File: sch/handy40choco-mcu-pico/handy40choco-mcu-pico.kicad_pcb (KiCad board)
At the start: 2 copper layers, 175 x 112 mm, 147 parts, among them J1 Conn_01x02, J2 Conn_02x08_Odd_Even, J3 USB_C_Receptacle_USB2.0_16P, J4 Conn_01x04, Q1 DMG2301L, SW1 SW_Push, SW10 SW_Push, SW11 SW_Push, SW12 SW_Push, SW13 SW_Push, SW14 SW_Push, SW15 SW_Push, SW16 SW_Push, SW17 SW_Push, SW18 SW_Push, SW19 SW_Push, SW2 SW_Push, SW20 SW_Push, SW21 SW_Push, SW22 SW_Push, SW23 SW_Push, SW24 SW_Push, SW25 SW_Push, SW26 SW_Push, SW27 SW_Push, SW28 SW_Push, SW29 SW_Push, SW3 SW_Push, SW30 SW_Push, SW31 SW_Push, SW32 SW_Push, SW33 SW_Push, SW34 SW_Push, SW35 SW_Push, SW36 SW_Push, SW37 SW_Push, SW38 SW_Push, SW39 SW_Push, SW4 SW_Push, SW40 SW_Push, SW41 SW_Push, SW42 SW_Push, SW5 SW_Push, SW6 SW_Push, SW7 SW_Push, SW8 SW_Push, SW9 SW_Push, U1 Pico, U2 pimoroni lcd, U3 ESP32-S3-WROOM-1, U4 MIC5219-3.3YM5, Y1 32k

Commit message: マイコン基板(pico)の雛形です。
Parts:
- removed C1: 10u, Capacitor_SMD:C_0603_1608Metric_Pad1.08x0.95mm_HandSolder
- removed C2, C3: 100n, Capacitor_SMD:C_0603_1608Metric_Pad1.08x0.95mm_HandSolder
- removed C4: 1u, Capacitor_SMD:C_0603_1608Metric_Pad1.08x0.95mm_HandSolder
- removed C5: 470p, Capacitor_SMD:C_0603_1608Metric_Pad1.08x0.95mm_HandSolder
- removed C6: 10n, Capacitor_SMD:C_0603_1608Metric_Pad1.08x0.95mm_HandSolder
- removed C7, C8: 15p, Capacitor_SMD:C_0603_1608Metric_Pad1.08x0.95mm_HandSolder
- removed D1, D10, D11, D12, D13, D14, D15, D16, D17, D18, D19, D2, D20, D21, D22, D23, D24, D25, D26, D27, D28, D29, D3, D30, D31, D32, D33, D34, D35, D36, D37, D38, D39, D4, D40, D5, D6, D7, D8, D9: 1N4148W, Diode_SMD:D_SOD-123
- removed D41, D42, D43: D_Schottky, Diode_SMD:D_SOD-123
- removed D44, D45, D46: D_TVS, Diode_SMD:D_SOD-123
- removed D47, D48, D49, D50, D51, D52, D53: LED, LED_SMD:LED_0603_1608Metric_Pad1.05x0.95mm_HandSolder
- removed F1: Polyfuse_Small, Fuse:Fuse_Littelfuse-NANO2-451_453
- removed H1, H10, H11, H12, H13, H14, H2, H3, H4, H5, H6, H7, H8, H9: MountingHole, my_keyswitch:my_MountingHole_2.2mm_M2
- removed J3: USB_C_Receptacle_USB2.0_16P, Connector_USB:USB_C_Receptacle_XKB_U262-16XN-4BVC11
- removed J4: Conn_01x04, Connector_JST:JST_XH_B4B-XH-A_1x04_P2.50mm_Vertical
- removed R1, R11, R12, R2, R8, R9: 0, Resistor_SMD:R_0603_1608Metric
- removed R10: [10M], Resistor_SMD:R_0603_1608Metric
- removed R13, R14, R15, R16, R17, R18, R19: 1k, Resistor_SMD:R_0603_1608Metric
- removed R3, R4, R7: 10k, Resistor_SMD:R_0603_1608Metric
- removed R5, R6: 5.1k, Resistor_SMD:R_0603_1608Metric
- removed SW1, SW10, SW11, SW12, SW13, SW14, SW15, SW16, SW17, SW18, SW19, SW2, SW20, SW21, SW22, SW23, SW24, SW25, SW26, SW27, SW28, SW29, SW3, SW30, SW31, SW32, SW33, SW34, SW35, SW36, SW37, SW38, SW39, SW4, SW40, SW5, SW6, SW7, SW8, SW9: SW_Push, my_keyswitch:SW_Hotswap_Kailh_Choc_V1V2
- removed SW41, SW42: SW_Push, Button_Switch_SMD:SW_Push_SPST_NO_Alps_SKRK
- removed U2: pimoroni lcd, my_pico:pimoroni_lcd_p0.85
- removed U3: ESP32-S3-WROOM-1, RF_Module:ESP32-S3-WROOM-1
- removed U4: MIC5219-3.3YM5, Package_TO_SOT_SMD:SOT-23-5
- removed Y1: 32k, Crystal:Crystal_SMD_2012-2Pin_2.0x1.2mm_HandSoldering
- J2: value Conn_02x08_Odd_Even -> Conn_01x20; footprint my_pico:oled_PinSocket_2x08_P2.54mm_Vertical -> Connector_PinSocket_2.54mm:PinSocket_1x20_P2.54mm_Vertical
- moved J2 98.9 mm to (235.0, 88.0), turned to -90 degrees
- moved Q1 39.3 mm to (170.0, 67.9)
- moved J1 29.8 mm to (172.5, 56.0)
- moved U1 24.2 mm to (210.9, 71.6)
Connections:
- J2 pad 1: GND -> /ROW3
- J2 pad 10: unconnected-(J2-Pin_10-Pad10) -> /COL8
- J2 pad 11: unconnected-(J2-Pin_11-Pad11) -> /COL7
- J2 pad 12: Net-(J2-Pin_12) -> /COL6
- J2 pad 13: Net-(J2-Pin_13) -> GND
- J2 pad 14: /DC -> /COL5
- J2 pad 15: /OLED_RESET -> /COL4
- J2 pad 16: /CS_N -> /COL3
- J2 pad 2: +3.3V -> /ROW2
- J2 pad 3: unconnected-(J2-Pin_3-Pad3) -> GND
- J2 pad 4: /SCLK -> /ROW1
- J2 pad 5: /DATA -> /ROW0
- J2 pad 6: unconnected-(J2-Pin_6-Pad6) -> /COL11
- J2 pad 7: unconnected-(J2-Pin_7-Pad7) -> /COL10
- J2 pad 8: unconnected-(J2-Pin_8-Pad8) -> GND
- J2 pad 9: unconnected-(J2-Pin_9-Pad9) -> /COL9
- U1 pad 1: unconnected-(U1-GPIO0-Pad1)_1 -> /ROW3
- U1 pad 2: unconnected-(U1-GPIO1-Pad2)_1 -> /ROW2
- U1 pad 21: /DC -> unconnected-(U1-GPIO16-Pad21)_1
- U1 pad 22: /CS_N -> unconnected-(U1-GPIO17-Pad22)
- U1 pad 24: /SCLK -> unconnected-(U1-GPIO18-Pad24)
- U1 pad 25: /DATA -> unconnected-(U1-GPIO19-Pad25)
- U1 pad 26: /LCD_BL -> unconnected-(U1-GPIO20-Pad26)
- U1 pad 27: /LCD_TE -> unconnected-(U1-GPIO21-Pad27)_1
- U1 pad 29: /OLED_RESET -> unconnected-(U1-GPIO22-Pad29)_1
- U1 pad 30: /LCD_RESET -> unconnected-(U1-RUN-Pad30)
- U1 pad 4: /ROW3 -> /ROW1
- U1 pad 5: /ROW2 -> /ROW0
- U1 pad 6: /ROW1 -> /COL11
- U1 pad 7: /ROW0 -> /COL10
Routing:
- net /ROW3: track 291.0 -> 0.00 mm, vias 10 -> 0
- net /ROW2: track 274.4 -> 0.00 mm, vias 10 -> 0
- net /ROW1: track 259.9 -> 0.00 mm, vias 10 -> 0
- net /ROW0: track 224.4 -> 0.00 mm, vias 10 -> 0
- net /COL0: track 216.7 -> 0.00 mm
- net /COL1: track 206.4 -> 0.00 mm
- net /COL2: track 186.6 -> 0.00 mm
- net /COL3: track 173.0 -> 0.00 mm
- net +3.3V: track 170.8 -> 0.00 mm, vias 3 -> 0
- net /COL4: track 155.4 -> 0.00 mm
- net /COL5: track 142.1 -> 0.00 mm
- net /COL6: track 132.1 -> 0.00 mm
- net /COL7: track 119.2 -> 0.00 mm
- net /LCD_RESET: track 111.5 -> 0.00 mm
- net /COL8: track 107.2 -> 0.00 mm
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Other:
- board size 175 x 112 mm -> 169.5 x 40 mm
- board text added: "handy40choco mcu pico rev.1"
- board text added: "https://github.com/kenyahiro/handy40choco"
- board text removed: "https://github.com/kenyahiro/mini48-keyboard"
- board text removed: "mini48-keyboard_v2_p17"

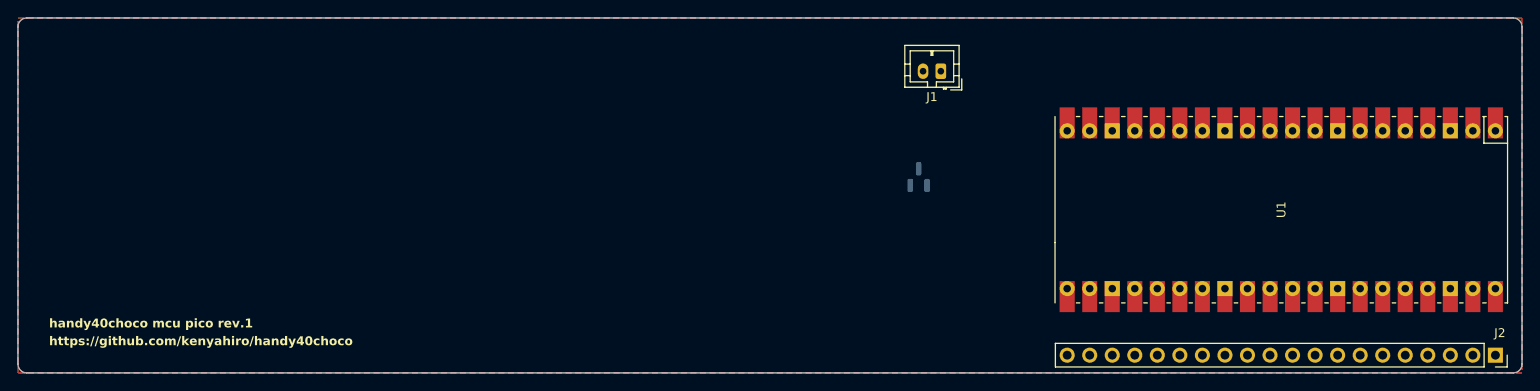
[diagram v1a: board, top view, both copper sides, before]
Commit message: OLEDのコネクタを追加しました。
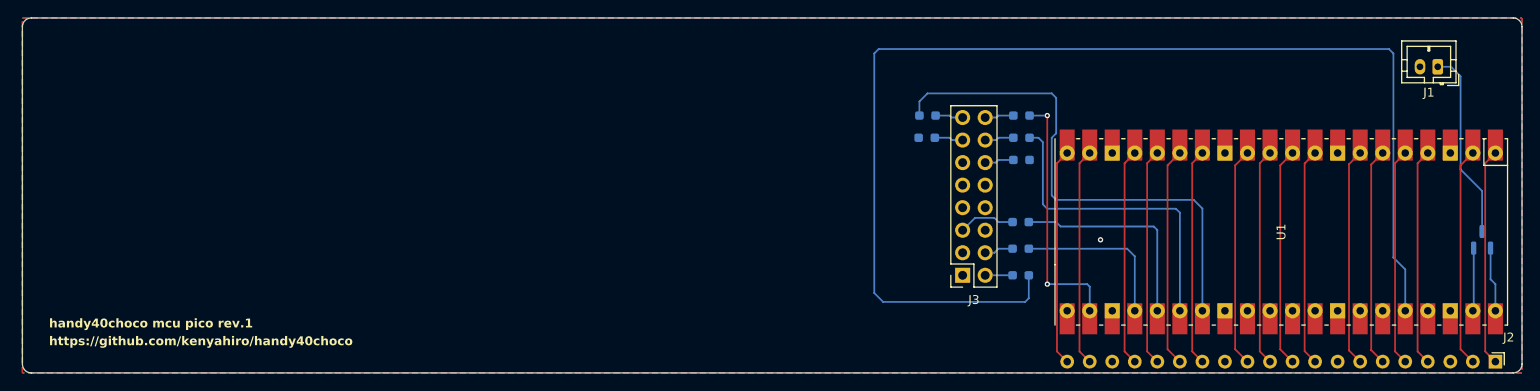
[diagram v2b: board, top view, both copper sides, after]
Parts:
- added J3: Conn_02x08_Odd_Even, my_pico:oled_PinSocket_2x08_P2.54mm_Vertical, F.Cu at (175.0, 79.0)
- added R1: 0, Resistor_SMD:R_0603_1608Metric_Pad0.98x0.95mm_HandSolder, B.Cu at (181.5, 79.0)
- added R2: 1k, Resistor_SMD:R_0603_1608Metric_Pad0.98x0.95mm_HandSolder, B.Cu at (181.6, 66.0)
- added R3: 1k, Resistor_SMD:R_0603_1608Metric_Pad0.98x0.95mm_HandSolder, B.Cu at (170.9, 63.5)
- added R4: 22, Resistor_SMD:R_0603_1608Metric_Pad0.98x0.95mm_HandSolder, B.Cu at (181.6, 61.0)
- added R5: 22, Resistor_SMD:R_0603_1608Metric_Pad0.98x0.95mm_HandSolder, B.Cu at (181.5, 76.0)
- added R6: 22, Resistor_SMD:R_0603_1608Metric_Pad0.98x0.95mm_HandSolder, B.Cu at (181.5, 73.0)
- added R7: 22, Resistor_SMD:R_0603_1608Metric_Pad0.98x0.95mm_HandSolder, B.Cu at (181.6, 63.5)
- added R8: 22, Resistor_SMD:R_0603_1608Metric_Pad0.98x0.95mm_HandSolder, B.Cu at (171.0, 61.0)
- J2: footprint Connector_PinSocket_2.54mm:PinSocket_1x20_P2.54mm_Vertical -> my_keyswitch:my_PinHeader_1x20_P2.54mm_Vertical_p0.85
- moved Q1 63.9 mm to (233.5, 75.0)
- moved J1 56.0 mm to (228.5, 55.5)
- moved U1 2.50 mm to (210.9, 74.1)
- moved J2 0.73 mm to (235.0, 88.7)
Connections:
- U1 pad 22: unconnected-(U1-GPIO17-Pad22) -> Net-(U1-GPIO17)
- U1 pad 24: unconnected-(U1-GPIO18-Pad24) -> Net-(U1-GPIO18)
- U1 pad 25: unconnected-(U1-GPIO19-Pad25) -> Net-(U1-GPIO19)
- U1 pad 26: unconnected-(U1-GPIO20-Pad26) -> Net-(U1-GPIO20)
- U1 pad 27: unconnected-(U1-GPIO21-Pad27)_1 -> Net-(U1-GPIO21)
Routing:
- net +3.3V: track 0.00 -> 136.1 mm
- net Net-(U1-GPIO21): track 0.00 -> 57.9 mm
- net Net-(U1-GPIO20): track 0.00 -> 35.6 mm
- net Net-(U1-GPIO17): track 0.00 -> 28.6 mm, vias 0 -> 2
- net /ROW2: track 0.00 -> 24.7 mm
- net /COL6: track 0.00 -> 24.7 mm
- net /COL4: track 0.00 -> 24.7 mm
- net /COL8: track 0.00 -> 24.7 mm
- net /COL11: track 0.00 -> 24.6 mm
- net /COL10: track 0.00 -> 24.6 mm
- net /COL9: track 0.00 -> 24.5 mm
- net /ROW3: track 0.00 -> 24.5 mm
- net /ROW0: track 0.00 -> 24.5 mm
- net /COL3: track 0.00 -> 24.5 mm
- net /COL2: track 0.00 -> 24.5 mm
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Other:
- board size 169.5 x 40 mm -> 169 x 40 mm

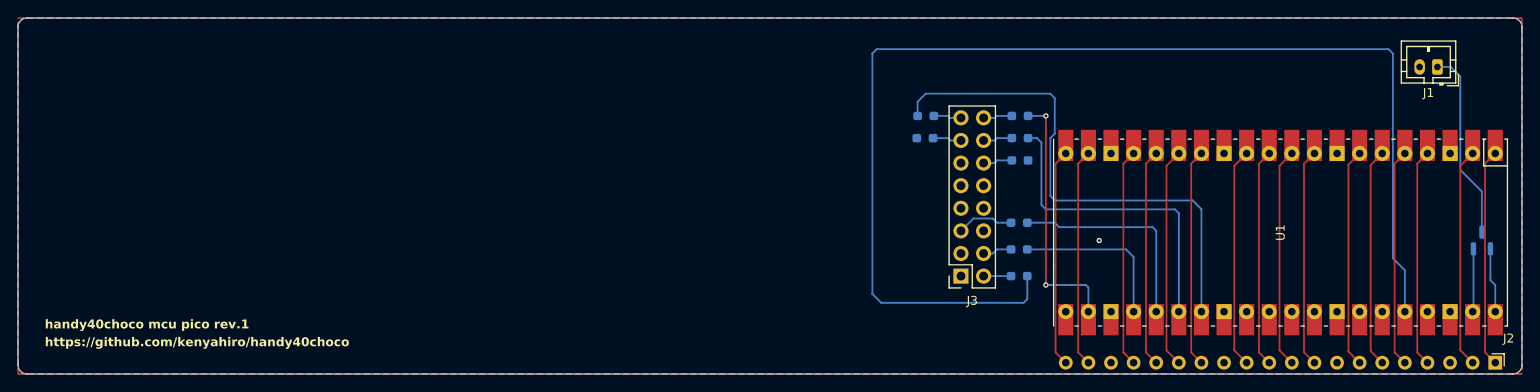
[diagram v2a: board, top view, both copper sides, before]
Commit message: ユニバーサル領域を追加しました。
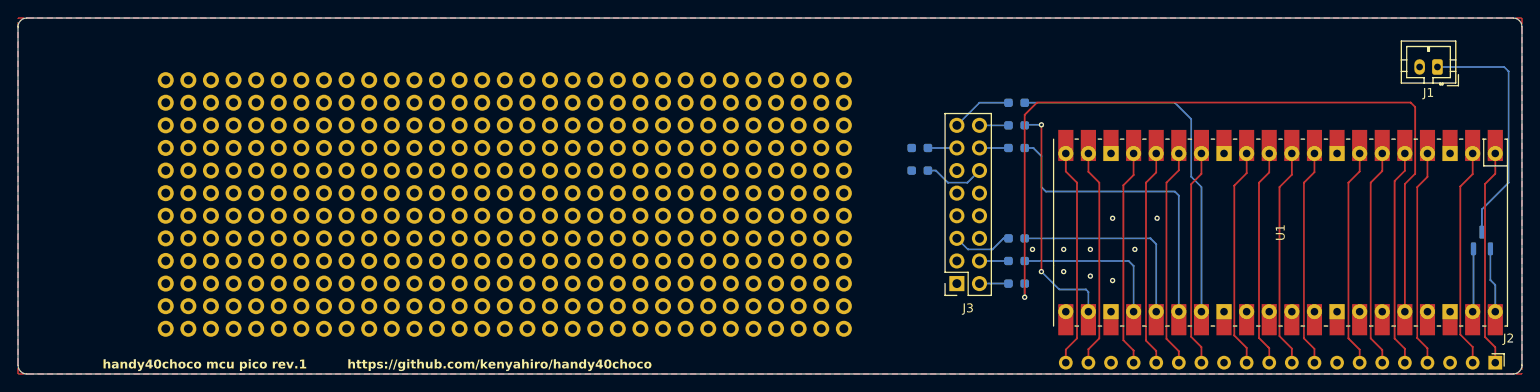
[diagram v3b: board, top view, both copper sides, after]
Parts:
- added H1: MountingHole_Pad, my_keyswitch:TestPoint_THTPad_a, F.Cu at (85.6, 57.0)
- added H10: MountingHole_Pad, my_keyswitch:TestPoint_THTPad_a, F.Cu at (85.6, 79.8)
- added H100: MountingHole_Pad, my_keyswitch:TestPoint_THTPad_a, F.Cu at (105.9, 64.6)
- added H101: MountingHole_Pad, my_keyswitch:TestPoint_THTPad_a, F.Cu at (105.9, 67.1)
- added H102: MountingHole_Pad, my_keyswitch:TestPoint_THTPad_a, F.Cu at (105.9, 69.7)
- added H103: MountingHole_Pad, my_keyswitch:TestPoint_THTPad_a, F.Cu at (105.9, 72.2)
- added H104: MountingHole_Pad, my_keyswitch:TestPoint_THTPad_a, F.Cu at (105.9, 74.8)
- added H105: MountingHole_Pad, my_keyswitch:TestPoint_THTPad_a, F.Cu at (105.9, 77.3)
- added H106: MountingHole_Pad, my_keyswitch:TestPoint_THTPad_a, F.Cu at (105.9, 79.8)
- added H107: MountingHole_Pad, my_keyswitch:TestPoint_THTPad_a, F.Cu at (105.9, 82.4)
- added H108: MountingHole_Pad, my_keyswitch:TestPoint_THTPad_a, F.Cu at (105.9, 84.9)
- added H109: MountingHole_Pad, my_keyswitch:TestPoint_THTPad_a, F.Cu at (108.5, 57.0)
- added H11: MountingHole_Pad, my_keyswitch:TestPoint_THTPad_a, F.Cu at (85.6, 82.4)
- added H110: MountingHole_Pad, my_keyswitch:TestPoint_THTPad_a, F.Cu at (108.5, 59.5)
- added H111: MountingHole_Pad, my_keyswitch:TestPoint_THTPad_a, F.Cu at (108.5, 62.1)
- added H112: MountingHole_Pad, my_keyswitch:TestPoint_THTPad_a, F.Cu at (108.5, 64.6)
- added H113: MountingHole_Pad, my_keyswitch:TestPoint_THTPad_a, F.Cu at (108.5, 67.1)
- added H114: MountingHole_Pad, my_keyswitch:TestPoint_THTPad_a, F.Cu at (108.5, 69.7)
- added H115: MountingHole_Pad, my_keyswitch:TestPoint_THTPad_a, F.Cu at (108.5, 72.2)
- added H116: MountingHole_Pad, my_keyswitch:TestPoint_THTPad_a, F.Cu at (108.5, 74.8)
- added H117: MountingHole_Pad, my_keyswitch:TestPoint_THTPad_a, F.Cu at (108.5, 77.3)
- added H118: MountingHole_Pad, my_keyswitch:TestPoint_THTPad_a, F.Cu at (108.5, 79.8)
- added H119: MountingHole_Pad, my_keyswitch:TestPoint_THTPad_a, F.Cu at (108.5, 82.4)
- added H12: MountingHole_Pad, my_keyswitch:TestPoint_THTPad_a, F.Cu at (85.6, 84.9)
- added H120: MountingHole_Pad, my_keyswitch:TestPoint_THTPad_a, F.Cu at (108.5, 84.9)
- added H121: MountingHole_Pad, my_keyswitch:TestPoint_THTPad_a, F.Cu at (111.0, 57.0)
- added H122: MountingHole_Pad, my_keyswitch:TestPoint_THTPad_a, F.Cu at (111.0, 59.5)
- added H123: MountingHole_Pad, my_keyswitch:TestPoint_THTPad_a, F.Cu at (111.0, 62.1)
- added H124: MountingHole_Pad, my_keyswitch:TestPoint_THTPad_a, F.Cu at (111.0, 64.6)
- added H125: MountingHole_Pad, my_keyswitch:TestPoint_THTPad_a, F.Cu at (111.0, 67.1)
- added H126: MountingHole_Pad, my_keyswitch:TestPoint_THTPad_a, F.Cu at (111.0, 69.7)
- added H127: MountingHole_Pad, my_keyswitch:TestPoint_THTPad_a, F.Cu at (111.0, 72.2)
- added H128: MountingHole_Pad, my_keyswitch:TestPoint_THTPad_a, F.Cu at (111.0, 74.8)
- added H129: MountingHole_Pad, my_keyswitch:TestPoint_THTPad_a, F.Cu at (111.0, 77.3)
- added H13: MountingHole_Pad, my_keyswitch:TestPoint_THTPad_a, F.Cu at (88.1, 57.0)
- added H130: MountingHole_Pad, my_keyswitch:TestPoint_THTPad_a, F.Cu at (111.0, 79.8)
- added H131: MountingHole_Pad, my_keyswitch:TestPoint_THTPad_a, F.Cu at (111.0, 82.4)
- added H132: MountingHole_Pad, my_keyswitch:TestPoint_THTPad_a, F.Cu at (111.0, 84.9)
- added H133: MountingHole_Pad, my_keyswitch:TestPoint_THTPad_a, F.Cu at (113.5, 57.0)
- added H134: MountingHole_Pad, my_keyswitch:TestPoint_THTPad_a, F.Cu at (113.5, 59.5)
- added H135: MountingHole_Pad, my_keyswitch:TestPoint_THTPad_a, F.Cu at (113.5, 62.1)
- added H136: MountingHole_Pad, my_keyswitch:TestPoint_THTPad_a, F.Cu at (113.5, 64.6)
- added H137: MountingHole_Pad, my_keyswitch:TestPoint_THTPad_a, F.Cu at (113.5, 67.1)
- added H138: MountingHole_Pad, my_keyswitch:TestPoint_THTPad_a, F.Cu at (113.5, 69.7)
- added H139: MountingHole_Pad, my_keyswitch:TestPoint_THTPad_a, F.Cu at (113.5, 72.2)
- added H14: MountingHole_Pad, my_keyswitch:TestPoint_THTPad_a, F.Cu at (88.1, 59.5)
- added H140: MountingHole_Pad, my_keyswitch:TestPoint_THTPad_a, F.Cu at (113.5, 74.8)
- added H141: MountingHole_Pad, my_keyswitch:TestPoint_THTPad_a, F.Cu at (113.5, 77.3)
- added H142: MountingHole_Pad, my_keyswitch:TestPoint_THTPad_a, F.Cu at (113.5, 79.8)
- added H143: MountingHole_Pad, my_keyswitch:TestPoint_THTPad_a, F.Cu at (113.5, 82.4)
- added H144: MountingHole_Pad, my_keyswitch:TestPoint_THTPad_a, F.Cu at (113.5, 84.9)
- added H145: MountingHole_Pad, my_keyswitch:TestPoint_THTPad_a, F.Cu at (116.1, 57.0)
- added H146: MountingHole_Pad, my_keyswitch:TestPoint_THTPad_a, F.Cu at (116.1, 59.5)
- added H147: MountingHole_Pad, my_keyswitch:TestPoint_THTPad_a, F.Cu at (116.1, 62.1)
- added H148: MountingHole_Pad, my_keyswitch:TestPoint_THTPad_a, F.Cu at (116.1, 64.6)
- added H149: MountingHole_Pad, my_keyswitch:TestPoint_THTPad_a, F.Cu at (116.1, 67.1)
- added H15: MountingHole_Pad, my_keyswitch:TestPoint_THTPad_a, F.Cu at (88.1, 62.1)
- added H150: MountingHole_Pad, my_keyswitch:TestPoint_THTPad_a, F.Cu at (116.1, 69.7)
- added H151: MountingHole_Pad, my_keyswitch:TestPoint_THTPad_a, F.Cu at (116.1, 72.2)
- added H152: MountingHole_Pad, my_keyswitch:TestPoint_THTPad_a, F.Cu at (116.1, 74.8)
- added H153: MountingHole_Pad, my_keyswitch:TestPoint_THTPad_a, F.Cu at (116.1, 77.3)
- added H154: MountingHole_Pad, my_keyswitch:TestPoint_THTPad_a, F.Cu at (116.1, 79.8)
- added H155: MountingHole_Pad, my_keyswitch:TestPoint_THTPad_a, F.Cu at (116.1, 82.4)
- added H156: MountingHole_Pad, my_keyswitch:TestPoint_THTPad_a, F.Cu at (116.1, 84.9)
- added H157: MountingHole_Pad, my_keyswitch:TestPoint_THTPad_a, F.Cu at (118.6, 57.0)
- added H158: MountingHole_Pad, my_keyswitch:TestPoint_THTPad_a, F.Cu at (118.6, 59.5)
- added H159: MountingHole_Pad, my_keyswitch:TestPoint_THTPad_a, F.Cu at (118.6, 62.1)
- added H16: MountingHole_Pad, my_keyswitch:TestPoint_THTPad_a, F.Cu at (88.1, 64.6)
- added H160: MountingHole_Pad, my_keyswitch:TestPoint_THTPad_a, F.Cu at (118.6, 64.6)
- added H161: MountingHole_Pad, my_keyswitch:TestPoint_THTPad_a, F.Cu at (118.6, 67.1)
- added H162: MountingHole_Pad, my_keyswitch:TestPoint_THTPad_a, F.Cu at (118.6, 69.7)
- added H163: MountingHole_Pad, my_keyswitch:TestPoint_THTPad_a, F.Cu at (118.6, 72.2)
- added H164: MountingHole_Pad, my_keyswitch:TestPoint_THTPad_a, F.Cu at (118.6, 74.8)
- added H165: MountingHole_Pad, my_keyswitch:TestPoint_THTPad_a, F.Cu at (118.6, 77.3)
- added H166: MountingHole_Pad, my_keyswitch:TestPoint_THTPad_a, F.Cu at (118.6, 79.8)
- added H167: MountingHole_Pad, my_keyswitch:TestPoint_THTPad_a, F.Cu at (118.6, 82.4)
- added H168: MountingHole_Pad, my_keyswitch:TestPoint_THTPad_a, F.Cu at (118.6, 84.9)
- added H169: MountingHole_Pad, my_keyswitch:TestPoint_THTPad_a, F.Cu at (121.2, 57.0)
- added H17: MountingHole_Pad, my_keyswitch:TestPoint_THTPad_a, F.Cu at (88.1, 67.1)
- added H170: MountingHole_Pad, my_keyswitch:TestPoint_THTPad_a, F.Cu at (121.2, 59.5)
- added H171: MountingHole_Pad, my_keyswitch:TestPoint_THTPad_a, F.Cu at (121.2, 62.1)
- added H172: MountingHole_Pad, my_keyswitch:TestPoint_THTPad_a, F.Cu at (121.2, 64.6)
- added H173: MountingHole_Pad, my_keyswitch:TestPoint_THTPad_a, F.Cu at (121.2, 67.1)
- added H174: MountingHole_Pad, my_keyswitch:TestPoint_THTPad_a, F.Cu at (121.2, 69.7)
- added H175: MountingHole_Pad, my_keyswitch:TestPoint_THTPad_a, F.Cu at (121.2, 72.2)
- added H176: MountingHole_Pad, my_keyswitch:TestPoint_THTPad_a, F.Cu at (121.2, 74.8)
- added H177: MountingHole_Pad, my_keyswitch:TestPoint_THTPad_a, F.Cu at (121.2, 77.3)
- added H178: MountingHole_Pad, my_keyswitch:TestPoint_THTPad_a, F.Cu at (121.2, 79.8)
- added H179: MountingHole_Pad, my_keyswitch:TestPoint_THTPad_a, F.Cu at (121.2, 82.4)
- added H18: MountingHole_Pad, my_keyswitch:TestPoint_THTPad_a, F.Cu at (88.1, 69.7)
- added H180: MountingHole_Pad, my_keyswitch:TestPoint_THTPad_a, F.Cu at (121.2, 84.9)
- added H181: MountingHole_Pad, my_keyswitch:TestPoint_THTPad_a, F.Cu at (123.7, 57.0)
- added H182: MountingHole_Pad, my_keyswitch:TestPoint_THTPad_a, F.Cu at (123.7, 59.5)
- added H183: MountingHole_Pad, my_keyswitch:TestPoint_THTPad_a, F.Cu at (123.7, 62.1)
- added H184: MountingHole_Pad, my_keyswitch:TestPoint_THTPad_a, F.Cu at (123.7, 64.6)
- added H185: MountingHole_Pad, my_keyswitch:TestPoint_THTPad_a, F.Cu at (123.7, 67.1)
- added H186: MountingHole_Pad, my_keyswitch:TestPoint_THTPad_a, F.Cu at (123.7, 69.7)
- added H187: MountingHole_Pad, my_keyswitch:TestPoint_THTPad_a, F.Cu at (123.7, 72.2)
- added H188: MountingHole_Pad, my_keyswitch:TestPoint_THTPad_a, F.Cu at (123.7, 74.8)
- added H189: MountingHole_Pad, my_keyswitch:TestPoint_THTPad_a, F.Cu at (123.7, 77.3)
- added H19: MountingHole_Pad, my_keyswitch:TestPoint_THTPad_a, F.Cu at (88.1, 72.2)
- added H190: MountingHole_Pad, my_keyswitch:TestPoint_THTPad_a, F.Cu at (123.7, 79.8)
- added H191: MountingHole_Pad, my_keyswitch:TestPoint_THTPad_a, F.Cu at (123.7, 82.4)
- added H192: MountingHole_Pad, my_keyswitch:TestPoint_THTPad_a, F.Cu at (123.7, 84.9)
- added H193: MountingHole_Pad, my_keyswitch:TestPoint_THTPad_a, F.Cu at (126.2, 57.0)
- added H194: MountingHole_Pad, my_keyswitch:TestPoint_THTPad_a, F.Cu at (126.2, 59.5)
- added H195: MountingHole_Pad, my_keyswitch:TestPoint_THTPad_a, F.Cu at (126.2, 62.1)
- added H196: MountingHole_Pad, my_keyswitch:TestPoint_THTPad_a, F.Cu at (126.2, 64.6)
- added H197: MountingHole_Pad, my_keyswitch:TestPoint_THTPad_a, F.Cu at (126.2, 67.1)
- added H198: MountingHole_Pad, my_keyswitch:TestPoint_THTPad_a, F.Cu at (126.2, 69.7)
- added H199: MountingHole_Pad, my_keyswitch:TestPoint_THTPad_a, F.Cu at (126.2, 72.2)
- added H2: MountingHole_Pad, my_keyswitch:TestPoint_THTPad_a, F.Cu at (85.6, 59.5)
- added H20: MountingHole_Pad, my_keyswitch:TestPoint_THTPad_a, F.Cu at (88.1, 74.8)
- added H200: MountingHole_Pad, my_keyswitch:TestPoint_THTPad_a, F.Cu at (126.2, 74.8)
- added H201: MountingHole_Pad, my_keyswitch:TestPoint_THTPad_a, F.Cu at (126.2, 77.3)
- added H202: MountingHole_Pad, my_keyswitch:TestPoint_THTPad_a, F.Cu at (126.2, 79.8)
- added H203: MountingHole_Pad, my_keyswitch:TestPoint_THTPad_a, F.Cu at (126.2, 82.4)
- added H204: MountingHole_Pad, my_keyswitch:TestPoint_THTPad_a, F.Cu at (126.2, 84.9)
- added H205: MountingHole_Pad, my_keyswitch:TestPoint_THTPad_a, F.Cu at (128.8, 57.0)
- added H206: MountingHole_Pad, my_keyswitch:TestPoint_THTPad_a, F.Cu at (128.8, 59.5)
- added H207: MountingHole_Pad, my_keyswitch:TestPoint_THTPad_a, F.Cu at (128.8, 62.1)
- added H208: MountingHole_Pad, my_keyswitch:TestPoint_THTPad_a, F.Cu at (128.8, 64.6)
- added H209: MountingHole_Pad, my_keyswitch:TestPoint_THTPad_a, F.Cu at (128.8, 67.1)
- added H21: MountingHole_Pad, my_keyswitch:TestPoint_THTPad_a, F.Cu at (88.1, 77.3)
- added H210: MountingHole_Pad, my_keyswitch:TestPoint_THTPad_a, F.Cu at (128.8, 69.7)
- added H211: MountingHole_Pad, my_keyswitch:TestPoint_THTPad_a, F.Cu at (128.8, 72.2)
- added H212: MountingHole_Pad, my_keyswitch:TestPoint_THTPad_a, F.Cu at (128.8, 74.8)
- added H213: MountingHole_Pad, my_keyswitch:TestPoint_THTPad_a, F.Cu at (128.8, 77.3)
- added H214: MountingHole_Pad, my_keyswitch:TestPoint_THTPad_a, F.Cu at (128.8, 79.8)
- added H215: MountingHole_Pad, my_keyswitch:TestPoint_THTPad_a, F.Cu at (128.8, 82.4)
- added H216: MountingHole_Pad, my_keyswitch:TestPoint_THTPad_a, F.Cu at (128.8, 84.9)
- added H217: MountingHole_Pad, my_keyswitch:TestPoint_THTPad_a, F.Cu at (131.3, 57.0)
- added H218: MountingHole_Pad, my_keyswitch:TestPoint_THTPad_a, F.Cu at (131.3, 59.5)
- added H219: MountingHole_Pad, my_keyswitch:TestPoint_THTPad_a, F.Cu at (131.3, 62.1)
- added H22: MountingHole_Pad, my_keyswitch:TestPoint_THTPad_a, F.Cu at (88.1, 79.8)
- added H220: MountingHole_Pad, my_keyswitch:TestPoint_THTPad_a, F.Cu at (131.3, 64.6)
- added H221: MountingHole_Pad, my_keyswitch:TestPoint_THTPad_a, F.Cu at (131.3, 67.1)
- added H222: MountingHole_Pad, my_keyswitch:TestPoint_THTPad_a, F.Cu at (131.3, 69.7)
- added H223: MountingHole_Pad, my_keyswitch:TestPoint_THTPad_a, F.Cu at (131.3, 72.2)
- added H224: MountingHole_Pad, my_keyswitch:TestPoint_THTPad_a, F.Cu at (131.3, 74.8)
- added H225: MountingHole_Pad, my_keyswitch:TestPoint_THTPad_a, F.Cu at (131.3, 77.3)
- added H226: MountingHole_Pad, my_keyswitch:TestPoint_THTPad_a, F.Cu at (131.3, 79.8)
- added H227: MountingHole_Pad, my_keyswitch:TestPoint_THTPad_a, F.Cu at (131.3, 82.4)
- added H228: MountingHole_Pad, my_keyswitch:TestPoint_THTPad_a, F.Cu at (131.3, 84.9)
- added H229: MountingHole_Pad, my_keyswitch:TestPoint_THTPad_a, F.Cu at (133.9, 57.0)
- added H23: MountingHole_Pad, my_keyswitch:TestPoint_THTPad_a, F.Cu at (88.1, 82.4)
- added H230: MountingHole_Pad, my_keyswitch:TestPoint_THTPad_a, F.Cu at (133.9, 59.5)
- added H231: MountingHole_Pad, my_keyswitch:TestPoint_THTPad_a, F.Cu at (133.9, 62.1)
- added H232: MountingHole_Pad, my_keyswitch:TestPoint_THTPad_a, F.Cu at (133.9, 64.6)
- added H233: MountingHole_Pad, my_keyswitch:TestPoint_THTPad_a, F.Cu at (133.9, 67.1)
- added H234: MountingHole_Pad, my_keyswitch:TestPoint_THTPad_a, F.Cu at (133.9, 69.7)
- added H235: MountingHole_Pad, my_keyswitch:TestPoint_THTPad_a, F.Cu at (133.9, 72.2)
- added H236: MountingHole_Pad, my_keyswitch:TestPoint_THTPad_a, F.Cu at (133.9, 74.8)
- added H237: MountingHole_Pad, my_keyswitch:TestPoint_THTPad_a, F.Cu at (133.9, 77.3)
- added H238: MountingHole_Pad, my_keyswitch:TestPoint_THTPad_a, F.Cu at (133.9, 79.8)
- added H239: MountingHole_Pad, my_keyswitch:TestPoint_THTPad_a, F.Cu at (133.9, 82.4)
- added H24: MountingHole_Pad, my_keyswitch:TestPoint_THTPad_a, F.Cu at (88.1, 84.9)
- added H240: MountingHole_Pad, my_keyswitch:TestPoint_THTPad_a, F.Cu at (133.9, 84.9)
- added H241: MountingHole_Pad, my_keyswitch:TestPoint_THTPad_a, F.Cu at (136.4, 57.0)
- added H242: MountingHole_Pad, my_keyswitch:TestPoint_THTPad_a, F.Cu at (136.4, 59.5)
- added H243: MountingHole_Pad, my_keyswitch:TestPoint_THTPad_a, F.Cu at (136.4, 62.1)
- added H244: MountingHole_Pad, my_keyswitch:TestPoint_THTPad_a, F.Cu at (136.4, 64.6)
- added H245: MountingHole_Pad, my_keyswitch:TestPoint_THTPad_a, F.Cu at (136.4, 67.1)
- added H246: MountingHole_Pad, my_keyswitch:TestPoint_THTPad_a, F.Cu at (136.4, 69.7)
- added H247: MountingHole_Pad, my_keyswitch:TestPoint_THTPad_a, F.Cu at (136.4, 72.2)
- added H248: MountingHole_Pad, my_keyswitch:TestPoint_THTPad_a, F.Cu at (136.4, 74.8)
- added H249: MountingHole_Pad, my_keyswitch:TestPoint_THTPad_a, F.Cu at (136.4, 77.3)
- added H25: MountingHole_Pad, my_keyswitch:TestPoint_THTPad_a, F.Cu at (90.7, 57.0)
- added H250: MountingHole_Pad, my_keyswitch:TestPoint_THTPad_a, F.Cu at (136.4, 79.8)
- added H251: MountingHole_Pad, my_keyswitch:TestPoint_THTPad_a, F.Cu at (136.4, 82.4)
- added H252: MountingHole_Pad, my_keyswitch:TestPoint_THTPad_a, F.Cu at (136.4, 84.9)
- added H253: MountingHole_Pad, my_keyswitch:TestPoint_THTPad_a, F.Cu at (138.9, 57.0)
- added H254: MountingHole_Pad, my_keyswitch:TestPoint_THTPad_a, F.Cu at (138.9, 59.5)
- added H255: MountingHole_Pad, my_keyswitch:TestPoint_THTPad_a, F.Cu at (138.9, 62.1)
- added H256: MountingHole_Pad, my_keyswitch:TestPoint_THTPad_a, F.Cu at (138.9, 64.6)
- added H257: MountingHole_Pad, my_keyswitch:TestPoint_THTPad_a, F.Cu at (138.9, 67.1)
- added H258: MountingHole_Pad, my_keyswitch:TestPoint_THTPad_a, F.Cu at (138.9, 69.7)
- added H259: MountingHole_Pad, my_keyswitch:TestPoint_THTPad_a, F.Cu at (138.9, 72.2)
- added H26: MountingHole_Pad, my_keyswitch:TestPoint_THTPad_a, F.Cu at (90.7, 59.5)
- added H260: MountingHole_Pad, my_keyswitch:TestPoint_THTPad_a, F.Cu at (138.9, 74.8)
- added H261: MountingHole_Pad, my_keyswitch:TestPoint_THTPad_a, F.Cu at (138.9, 77.3)
- added H262: MountingHole_Pad, my_keyswitch:TestPoint_THTPad_a, F.Cu at (138.9, 79.8)
- added H263: MountingHole_Pad, my_keyswitch:TestPoint_THTPad_a, F.Cu at (138.9, 82.4)
- added H264: MountingHole_Pad, my_keyswitch:TestPoint_THTPad_a, F.Cu at (138.9, 84.9)
- added H265: MountingHole_Pad, my_keyswitch:TestPoint_THTPad_a, F.Cu at (141.5, 57.0)
- added H266: MountingHole_Pad, my_keyswitch:TestPoint_THTPad_a, F.Cu at (141.5, 59.5)
- added H267: MountingHole_Pad, my_keyswitch:TestPoint_THTPad_a, F.Cu at (141.5, 62.1)
- added H268: MountingHole_Pad, my_keyswitch:TestPoint_THTPad_a, F.Cu at (141.5, 64.6)
- added H269: MountingHole_Pad, my_keyswitch:TestPoint_THTPad_a, F.Cu at (141.5, 67.1)
- added H27: MountingHole_Pad, my_keyswitch:TestPoint_THTPad_a, F.Cu at (90.7, 62.1)
- added H270: MountingHole_Pad, my_keyswitch:TestPoint_THTPad_a, F.Cu at (141.5, 69.7)
- added H271: MountingHole_Pad, my_keyswitch:TestPoint_THTPad_a, F.Cu at (141.5, 72.2)
- added H272: MountingHole_Pad, my_keyswitch:TestPoint_THTPad_a, F.Cu at (141.5, 74.8)
- added H273: MountingHole_Pad, my_keyswitch:TestPoint_THTPad_a, F.Cu at (141.5, 77.3)
- added H274: MountingHole_Pad, my_keyswitch:TestPoint_THTPad_a, F.Cu at (141.5, 79.8)
- added H275: MountingHole_Pad, my_keyswitch:TestPoint_THTPad_a, F.Cu at (141.5, 82.4)
- added H276: MountingHole_Pad, my_keyswitch:TestPoint_THTPad_a, F.Cu at (141.5, 84.9)
- added H277: MountingHole_Pad, my_keyswitch:TestPoint_THTPad_a, F.Cu at (144.0, 57.0)
- added H278: MountingHole_Pad, my_keyswitch:TestPoint_THTPad_a, F.Cu at (144.0, 59.5)
- added H279: MountingHole_Pad, my_keyswitch:TestPoint_THTPad_a, F.Cu at (144.0, 62.1)
- added H28: MountingHole_Pad, my_keyswitch:TestPoint_THTPad_a, F.Cu at (90.7, 64.6)
- added H280: MountingHole_Pad, my_keyswitch:TestPoint_THTPad_a, F.Cu at (144.0, 64.6)
- added H281: MountingHole_Pad, my_keyswitch:TestPoint_THTPad_a, F.Cu at (144.0, 67.1)
- added H282: MountingHole_Pad, my_keyswitch:TestPoint_THTPad_a, F.Cu at (144.0, 69.7)
- added H283: MountingHole_Pad, my_keyswitch:TestPoint_THTPad_a, F.Cu at (144.0, 72.2)
- added H284: MountingHole_Pad, my_keyswitch:TestPoint_THTPad_a, F.Cu at (144.0, 74.8)
- added H285: MountingHole_Pad, my_keyswitch:TestPoint_THTPad_a, F.Cu at (144.0, 77.3)
- added H286: MountingHole_Pad, my_keyswitch:TestPoint_THTPad_a, F.Cu at (144.0, 79.8)
- added H287: MountingHole_Pad, my_keyswitch:TestPoint_THTPad_a, F.Cu at (144.0, 82.4)
- added H288: MountingHole_Pad, my_keyswitch:TestPoint_THTPad_a, F.Cu at (144.0, 84.9)
- added H289: MountingHole_Pad, my_keyswitch:TestPoint_THTPad_a, F.Cu at (146.6, 57.0)
- added H29: MountingHole_Pad, my_keyswitch:TestPoint_THTPad_a, F.Cu at (90.7, 67.1)
- added H290: MountingHole_Pad, my_keyswitch:TestPoint_THTPad_a, F.Cu at (146.6, 59.5)
- added H291: MountingHole_Pad, my_keyswitch:TestPoint_THTPad_a, F.Cu at (146.6, 62.1)
- added H292: MountingHole_Pad, my_keyswitch:TestPoint_THTPad_a, F.Cu at (146.6, 64.6)
- added H293: MountingHole_Pad, my_keyswitch:TestPoint_THTPad_a, F.Cu at (146.6, 67.1)
- added H294: MountingHole_Pad, my_keyswitch:TestPoint_THTPad_a, F.Cu at (146.6, 69.7)
- added H295: MountingHole_Pad, my_keyswitch:TestPoint_THTPad_a, F.Cu at (146.6, 72.2)
- added H296: MountingHole_Pad, my_keyswitch:TestPoint_THTPad_a, F.Cu at (146.6, 74.8)
- added H297: MountingHole_Pad, my_keyswitch:TestPoint_THTPad_a, F.Cu at (146.6, 77.3)
- added H298: MountingHole_Pad, my_keyswitch:TestPoint_THTPad_a, F.Cu at (146.6, 79.8)
- added H299: MountingHole_Pad, my_keyswitch:TestPoint_THTPad_a, F.Cu at (146.6, 82.4)
- added H3: MountingHole_Pad, my_keyswitch:TestPoint_THTPad_a, F.Cu at (85.6, 62.1)
- added H30: MountingHole_Pad, my_keyswitch:TestPoint_THTPad_a, F.Cu at (90.7, 69.7)
- added H300: MountingHole_Pad, my_keyswitch:TestPoint_THTPad_a, F.Cu at (146.6, 84.9)
- added H301: MountingHole_Pad, my_keyswitch:TestPoint_THTPad_a, F.Cu at (149.1, 57.0)
- added H302: MountingHole_Pad, my_keyswitch:TestPoint_THTPad_a, F.Cu at (149.1, 59.5)
- added H303: MountingHole_Pad, my_keyswitch:TestPoint_THTPad_a, F.Cu at (149.1, 62.1)
- added H304: MountingHole_Pad, my_keyswitch:TestPoint_THTPad_a, F.Cu at (149.1, 64.6)
- added H305: MountingHole_Pad, my_keyswitch:TestPoint_THTPad_a, F.Cu at (149.1, 67.1)
- added H306: MountingHole_Pad, my_keyswitch:TestPoint_THTPad_a, F.Cu at (149.1, 69.7)
- added H307: MountingHole_Pad, my_keyswitch:TestPoint_THTPad_a, F.Cu at (149.1, 72.2)
- added H308: MountingHole_Pad, my_keyswitch:TestPoint_THTPad_a, F.Cu at (149.1, 74.8)
- added H309: MountingHole_Pad, my_keyswitch:TestPoint_THTPad_a, F.Cu at (149.1, 77.3)
- added H31: MountingHole_Pad, my_keyswitch:TestPoint_THTPad_a, F.Cu at (90.7, 72.2)
- added H310: MountingHole_Pad, my_keyswitch:TestPoint_THTPad_a, F.Cu at (149.1, 79.8)
- added H311: MountingHole_Pad, my_keyswitch:TestPoint_THTPad_a, F.Cu at (149.1, 82.4)
- added H312: MountingHole_Pad, my_keyswitch:TestPoint_THTPad_a, F.Cu at (149.1, 84.9)
- added H313: MountingHole_Pad, my_keyswitch:TestPoint_THTPad_a, F.Cu at (151.6, 57.0)
- added H314: MountingHole_Pad, my_keyswitch:TestPoint_THTPad_a, F.Cu at (151.6, 59.5)
- added H315: MountingHole_Pad, my_keyswitch:TestPoint_THTPad_a, F.Cu at (151.6, 62.1)
- added H316: MountingHole_Pad, my_keyswitch:TestPoint_THTPad_a, F.Cu at (151.6, 64.6)
- added H317: MountingHole_Pad, my_keyswitch:TestPoint_THTPad_a, F.Cu at (151.6, 67.1)
- added H318: MountingHole_Pad, my_keyswitch:TestPoint_THTPad_a, F.Cu at (151.6, 69.7)
- added H319: MountingHole_Pad, my_keyswitch:TestPoint_THTPad_a, F.Cu at (151.6, 72.2)
- added H32: MountingHole_Pad, my_keyswitch:TestPoint_THTPad_a, F.Cu at (90.7, 74.8)
- added H320: MountingHole_Pad, my_keyswitch:TestPoint_THTPad_a, F.Cu at (151.6, 74.8)
- added H321: MountingHole_Pad, my_keyswitch:TestPoint_THTPad_a, F.Cu at (151.6, 77.3)
- added H322: MountingHole_Pad, my_keyswitch:TestPoint_THTPad_a, F.Cu at (151.6, 79.8)
- added H323: MountingHole_Pad, my_keyswitch:TestPoint_THTPad_a, F.Cu at (151.6, 82.4)
- added H324: MountingHole_Pad, my_keyswitch:TestPoint_THTPad_a, F.Cu at (151.6, 84.9)
- added H325: MountingHole_Pad, my_keyswitch:TestPoint_THTPad_a, F.Cu at (154.2, 57.0)
- added H326: MountingHole_Pad, my_keyswitch:TestPoint_THTPad_a, F.Cu at (154.2, 59.5)
- added H327: MountingHole_Pad, my_keyswitch:TestPoint_THTPad_a, F.Cu at (154.2, 62.1)
- added H328: MountingHole_Pad, my_keyswitch:TestPoint_THTPad_a, F.Cu at (154.2, 64.6)
- added H329: MountingHole_Pad, my_keyswitch:TestPoint_THTPad_a, F.Cu at (154.2, 67.1)
- added H33: MountingHole_Pad, my_keyswitch:TestPoint_THTPad_a, F.Cu at (90.7, 77.3)
- added H330: MountingHole_Pad, my_keyswitch:TestPoint_THTPad_a, F.Cu at (154.2, 69.7)
- added H331: MountingHole_Pad, my_keyswitch:TestPoint_THTPad_a, F.Cu at (154.2, 72.2)
- added H332: MountingHole_Pad, my_keyswitch:TestPoint_THTPad_a, F.Cu at (154.2, 74.8)
- added H333: MountingHole_Pad, my_keyswitch:TestPoint_THTPad_a, F.Cu at (154.2, 77.3)
- added H334: MountingHole_Pad, my_keyswitch:TestPoint_THTPad_a, F.Cu at (154.2, 79.8)
- added H335: MountingHole_Pad, my_keyswitch:TestPoint_THTPad_a, F.Cu at (154.2, 82.4)
- added H336: MountingHole_Pad, my_keyswitch:TestPoint_THTPad_a, F.Cu at (154.2, 84.9)
- added H337: MountingHole_Pad, my_keyswitch:TestPoint_THTPad_a, F.Cu at (156.7, 57.0)
- added H338: MountingHole_Pad, my_keyswitch:TestPoint_THTPad_a, F.Cu at (156.7, 59.5)
- added H339: MountingHole_Pad, my_keyswitch:TestPoint_THTPad_a, F.Cu at (156.7, 62.1)
- added H34: MountingHole_Pad, my_keyswitch:TestPoint_THTPad_a, F.Cu at (90.7, 79.8)
- added H340: MountingHole_Pad, my_keyswitch:TestPoint_THTPad_a, F.Cu at (156.7, 64.6)
- added H341: MountingHole_Pad, my_keyswitch:TestPoint_THTPad_a, F.Cu at (156.7, 67.1)
- added H342: MountingHole_Pad, my_keyswitch:TestPoint_THTPad_a, F.Cu at (156.7, 69.7)
- added H343: MountingHole_Pad, my_keyswitch:TestPoint_THTPad_a, F.Cu at (156.7, 72.2)
- added H344: MountingHole_Pad, my_keyswitch:TestPoint_THTPad_a, F.Cu at (156.7, 74.8)
- added H345: MountingHole_Pad, my_keyswitch:TestPoint_THTPad_a, F.Cu at (156.7, 77.3)
- added H346: MountingHole_Pad, my_keyswitch:TestPoint_THTPad_a, F.Cu at (156.7, 79.8)
- added H347: MountingHole_Pad, my_keyswitch:TestPoint_THTPad_a, F.Cu at (156.7, 82.4)
- added H348: MountingHole_Pad, my_keyswitch:TestPoint_THTPad_a, F.Cu at (156.7, 84.9)
- added H349: MountingHole_Pad, my_keyswitch:TestPoint_THTPad_a, F.Cu at (159.3, 57.0)
- added H35: MountingHole_Pad, my_keyswitch:TestPoint_THTPad_a, F.Cu at (90.7, 82.4)
- added H350: MountingHole_Pad, my_keyswitch:TestPoint_THTPad_a, F.Cu at (159.3, 59.5)
- added H351: MountingHole_Pad, my_keyswitch:TestPoint_THTPad_a, F.Cu at (159.3, 62.1)
- added H352: MountingHole_Pad, my_keyswitch:TestPoint_THTPad_a, F.Cu at (159.3, 64.6)
- added H353: MountingHole_Pad, my_keyswitch:TestPoint_THTPad_a, F.Cu at (159.3, 67.1)
- added H354: MountingHole_Pad, my_keyswitch:TestPoint_THTPad_a, F.Cu at (159.3, 69.7)
- added H355: MountingHole_Pad, my_keyswitch:TestPoint_THTPad_a, F.Cu at (159.3, 72.2)
- added H356: MountingHole_Pad, my_keyswitch:TestPoint_THTPad_a, F.Cu at (159.3, 74.8)
- added H357: MountingHole_Pad, my_keyswitch:TestPoint_THTPad_a, F.Cu at (159.3, 77.3)
- added H358: MountingHole_Pad, my_keyswitch:TestPoint_THTPad_a, F.Cu at (159.3, 79.8)
- added H359: MountingHole_Pad, my_keyswitch:TestPoint_THTPad_a, F.Cu at (159.3, 82.4)
- added H36: MountingHole_Pad, my_keyswitch:TestPoint_THTPad_a, F.Cu at (90.7, 84.9)
- added H360: MountingHole_Pad, my_keyswitch:TestPoint_THTPad_a, F.Cu at (159.3, 84.9)
- added H361: MountingHole_Pad, my_keyswitch:TestPoint_THTPad_a, F.Cu at (161.8, 57.0)
- added H362: MountingHole_Pad, my_keyswitch:TestPoint_THTPad_a, F.Cu at (161.8, 59.5)
- added H363: MountingHole_Pad, my_keyswitch:TestPoint_THTPad_a, F.Cu at (161.8, 62.1)
- added H364: MountingHole_Pad, my_keyswitch:TestPoint_THTPad_a, F.Cu at (161.8, 64.6)
- added H365: MountingHole_Pad, my_keyswitch:TestPoint_THTPad_a, F.Cu at (161.8, 67.1)
- added H366: MountingHole_Pad, my_keyswitch:TestPoint_THTPad_a, F.Cu at (161.8, 69.7)
- added H367: MountingHole_Pad, my_keyswitch:TestPoint_THTPad_a, F.Cu at (161.8, 72.2)
- added H368: MountingHole_Pad, my_keyswitch:TestPoint_THTPad_a, F.Cu at (161.8, 74.8)
- added H369: MountingHole_Pad, my_keyswitch:TestPoint_THTPad_a, F.Cu at (161.8, 77.3)
- added H37: MountingHole_Pad, my_keyswitch:TestPoint_THTPad_a, F.Cu at (93.2, 57.0)
- added H370: MountingHole_Pad, my_keyswitch:TestPoint_THTPad_a, F.Cu at (161.8, 79.8)
- added H371: MountingHole_Pad, my_keyswitch:TestPoint_THTPad_a, F.Cu at (161.8, 82.4)
- added H372: MountingHole_Pad, my_keyswitch:TestPoint_THTPad_a, F.Cu at (161.8, 84.9)
- added H38: MountingHole_Pad, my_keyswitch:TestPoint_THTPad_a, F.Cu at (93.2, 59.5)
- added H39: MountingHole_Pad, my_keyswitch:TestPoint_THTPad_a, F.Cu at (93.2, 62.1)
- added H4: MountingHole_Pad, my_keyswitch:TestPoint_THTPad_a, F.Cu at (85.6, 64.6)
- added H40: MountingHole_Pad, my_keyswitch:TestPoint_THTPad_a, F.Cu at (93.2, 64.6)
- added H41: MountingHole_Pad, my_keyswitch:TestPoint_THTPad_a, F.Cu at (93.2, 67.1)
- added H42: MountingHole_Pad, my_keyswitch:TestPoint_THTPad_a, F.Cu at (93.2, 69.7)
- added H43: MountingHole_Pad, my_keyswitch:TestPoint_THTPad_a, F.Cu at (93.2, 72.2)
- added H44: MountingHole_Pad, my_keyswitch:TestPoint_THTPad_a, F.Cu at (93.2, 74.8)
- added H45: MountingHole_Pad, my_keyswitch:TestPoint_THTPad_a, F.Cu at (93.2, 77.3)
- added H46: MountingHole_Pad, my_keyswitch:TestPoint_THTPad_a, F.Cu at (93.2, 79.8)
- added H47: MountingHole_Pad, my_keyswitch:TestPoint_THTPad_a, F.Cu at (93.2, 82.4)
- added H48: MountingHole_Pad, my_keyswitch:TestPoint_THTPad_a, F.Cu at (93.2, 84.9)
- added H49: MountingHole_Pad, my_keyswitch:TestPoint_THTPad_a, F.Cu at (95.8, 57.0)
- added H5: MountingHole_Pad, my_keyswitch:TestPoint_THTPad_a, F.Cu at (85.6, 67.1)
- added H50: MountingHole_Pad, my_keyswitch:TestPoint_THTPad_a, F.Cu at (95.8, 59.5)
- added H51: MountingHole_Pad, my_keyswitch:TestPoint_THTPad_a, F.Cu at (95.8, 62.1)
- added H52: MountingHole_Pad, my_keyswitch:TestPoint_THTPad_a, F.Cu at (95.8, 64.6)
- added H53: MountingHole_Pad, my_keyswitch:TestPoint_THTPad_a, F.Cu at (95.8, 67.1)
- added H54: MountingHole_Pad, my_keyswitch:TestPoint_THTPad_a, F.Cu at (95.8, 69.7)
- added H55: MountingHole_Pad, my_keyswitch:TestPoint_THTPad_a, F.Cu at (95.8, 72.2)
- added H56: MountingHole_Pad, my_keyswitch:TestPoint_THTPad_a, F.Cu at (95.8, 74.8)
- added H57: MountingHole_Pad, my_keyswitch:TestPoint_THTPad_a, F.Cu at (95.8, 77.3)
- added H58: MountingHole_Pad, my_keyswitch:TestPoint_THTPad_a, F.Cu at (95.8, 79.8)
- added H59: MountingHole_Pad, my_keyswitch:TestPoint_THTPad_a, F.Cu at (95.8, 82.4)
- added H6: MountingHole_Pad, my_keyswitch:TestPoint_THTPad_a, F.Cu at (85.6, 69.7)
- added H60: MountingHole_Pad, my_keyswitch:TestPoint_THTPad_a, F.Cu at (95.8, 84.9)
- added H61: MountingHole_Pad, my_keyswitch:TestPoint_THTPad_a, F.Cu at (98.3, 57.0)
- added H62: MountingHole_Pad, my_keyswitch:TestPoint_THTPad_a, F.Cu at (98.3, 59.5)
- added H63: MountingHole_Pad, my_keyswitch:TestPoint_THTPad_a, F.Cu at (98.3, 62.1)
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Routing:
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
